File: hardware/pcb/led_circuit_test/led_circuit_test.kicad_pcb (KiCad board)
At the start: 2 copper layers, 59.7 x 17.8 mm, 23 parts, among them J1 Conn_01x01_Male, J2 Conn_01x01_Male, J3 Conn_01x01_Male, J4 Conn_01x01_Male, J5 Conn_01x01_Male, J6 Conn_01x01_Male

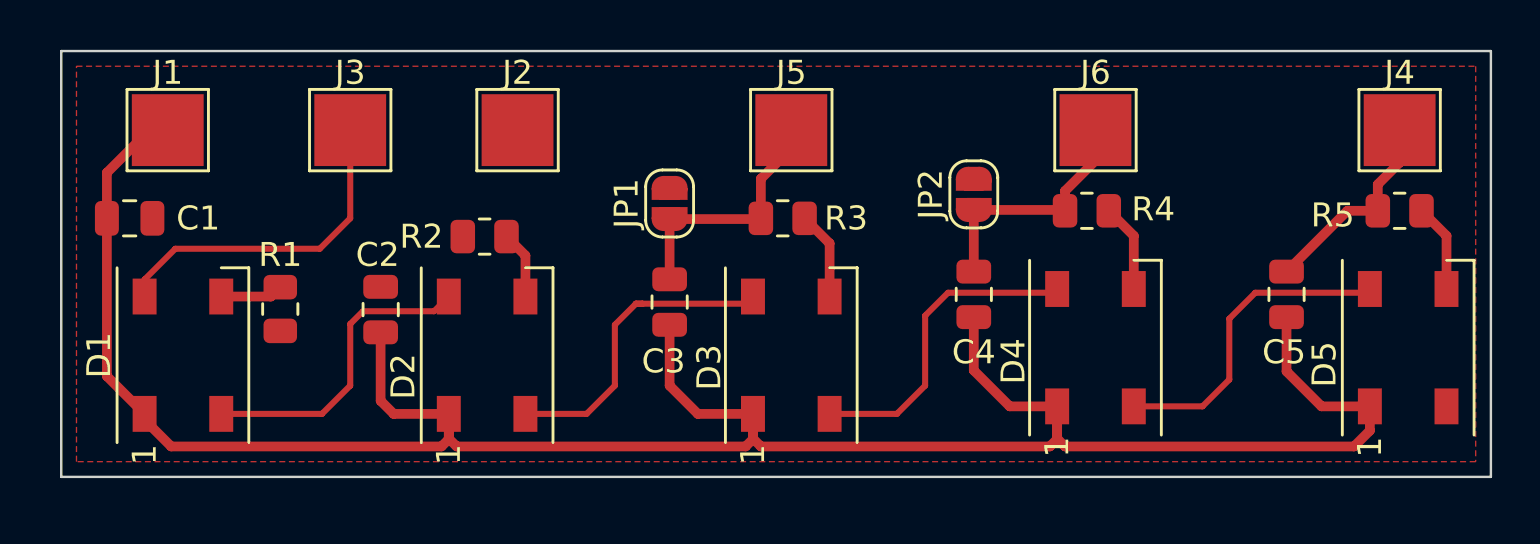
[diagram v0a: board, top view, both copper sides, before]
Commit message: Updated and enhanced test PCB after testing
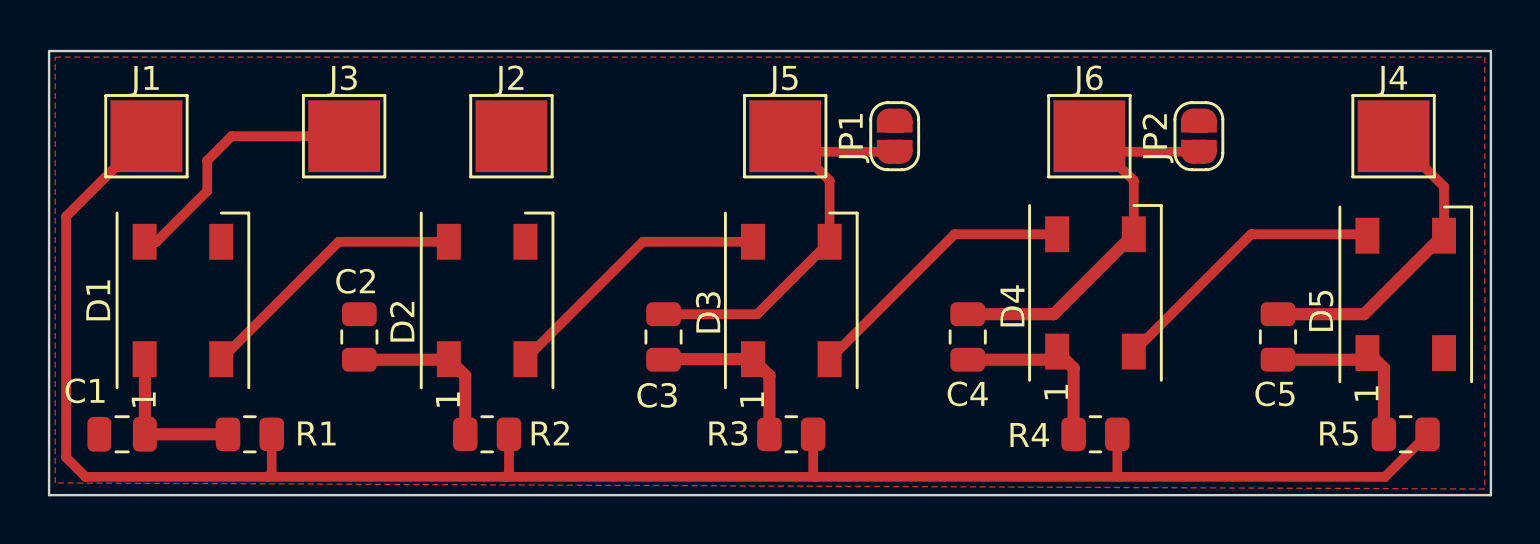
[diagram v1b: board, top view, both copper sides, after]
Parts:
- moved JP1 9.81 mm to (111.0, 29.0)
- moved JP2 9.71 mm to (123.7, 29.0)
- moved R4 9.34 mm to (119.4, 41.4), turned to 0 degrees
- moved R5 9.34 mm to (132.3, 41.4), turned to 0 degrees
- moved R3 9.02 mm to (106.7, 41.4), turned to 0 degrees
- moved C1 9.02 mm to (78.7, 41.4), turned to 180 degrees
- moved R2 8.26 mm to (94.0, 41.4), turned to 0 degrees
- moved R1 5.38 mm to (84.1, 41.4), turned to 0 degrees
- moved D1 2.29 mm to (81.3, 35.8)
- moved D2 2.29 mm to (94.0, 35.8)
- moved D3 2.29 mm to (106.7, 35.8)
- moved D4 2.29 mm to (119.4, 35.5)
- moved D5 2.23 mm to (132.3, 35.6)
- moved C5 1.81 mm to (127.0, 37.3)
- moved C4 1.80 mm to (114.0, 37.3)
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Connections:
- C1 pad 1: +5V -> Net-(C1-Pad1)
- C2 pad 1: +5V -> Net-(C2-Pad1)
- C3 pad 1: +5V -> Net-(C3-Pad1)
- C4 pad 1: +5V -> Net-(C4-Pad1)
- C5 pad 1: +5V -> Net-(C5-Pad1)
- D1 pad 1: +5V -> Net-(C1-Pad1)
- D1 pad 3: Net-(D1-Pad3) -> GND
- D2 pad 1: +5V -> Net-(C2-Pad1)
- D2 pad 3: Net-(D2-Pad3) -> GND
- D3 pad 1: +5V -> Net-(C3-Pad1)
- D3 pad 3: Net-(D3-Pad3) -> Net-(C3-Pad2)
- D4 pad 1: +5V -> Net-(C4-Pad1)
- D4 pad 3: Net-(D4-Pad3) -> Net-(C4-Pad2)
- D5 pad 1: +5V -> Net-(C5-Pad1)
- D5 pad 3: Net-(D5-Pad3) -> Net-(C5-Pad2)
- R1 pad 1: Net-(D1-Pad3) -> Net-(C1-Pad1)
- R1 pad 2: GND -> +5V
- R2 pad 1: Net-(D2-Pad3) -> Net-(C2-Pad1)
- R2 pad 2: GND -> +5V
- R3 pad 1: Net-(D3-Pad3) -> Net-(C3-Pad1)
- R3 pad 2: Net-(C3-Pad2) -> +5V
- R4 pad 1: Net-(D4-Pad3) -> Net-(C4-Pad1)
- R4 pad 2: Net-(C4-Pad2) -> +5V
- R5 pad 1: Net-(D5-Pad3) -> Net-(C5-Pad1)
- R5 pad 2: Net-(C5-Pad2) -> +5V
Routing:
- net +5V: track 100.3 -> 80.0 mm
- net Net-(C5-Pad1): track 0.00 -> 7.61 mm
- net Net-(C4-Pad1): track 0.00 -> 7.61 mm
- net Net-(C3-Pad1): track 0.00 -> 7.17 mm
- net Net-(C2-Pad1): track 0.00 -> 7.17 mm
- net Net-(C4-Pad2): track 11.1 -> 18.0 mm
- net Net-(C3-Pad2): track 11.3 -> 18.2 mm
- net Net-(C1-Pad1): track 0.00 -> 6.61 mm
- net Net-(C5-Pad2): track 9.37 -> 13.3 mm
- net Net-(D1-Pad4): track 14.8 -> 10.9 mm
- net Net-(D4-Pad3): track 3.70 -> 0.00 mm
- net Net-(D3-Pad3): track 3.70 -> 0.00 mm
- net Net-(D5-Pad3): track 3.70 -> 0.00 mm
- net Net-(D2-Pad3): track 2.83 -> 0.00 mm
- net Net-(D1-Pad3): track 2.63 -> 0.00 mm
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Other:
- board size 59.7 x 17.8 mm -> 60.2 x 18.5 mm
